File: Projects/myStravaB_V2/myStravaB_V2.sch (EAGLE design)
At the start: 103 parts, among them IC1 TPS63051RMWT, Q2 BSS138BKW, T1 BC847, T2 BC847, U1 FXOS8700CQR1, U2 MCP73831, U4 NRF52840, Y2 16MHz, Y3 32.768kHz

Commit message: Final design
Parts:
- added U$8: NET_CONN, NET_CONN:NET_CONN
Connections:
- new net N$10: C35.2, U$8.2, U4.VSS_PA
- net GND: now also U$8.1; no longer C35.2, U4.VSS_PA

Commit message: Added speaker
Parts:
- added C18: 1uF, rcl:C-EUC0603
- added C19: DNP, rcl:C-EUC0805
- added R28: 10k, rcl:R-US_R0603
- added R29: 330, rcl:R-US_R0603
- added T3: BC847, transistor:BC847
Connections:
- removed net XX: U4.P26
- new net N$11: R28.2, T3.B
- new net N$18: C18.2, C19.2
- new net N$6: C18.1, R29.1, T3.C
- new net SPK_IN: R28.1, U4.P26
- net GND: now also C19.1, T3.E
- net VCC: now also R29.2

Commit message: Some fuckups corrected
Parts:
- C35: value 820pF -> 0.8pF
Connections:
- removed net YY: U4.P4
- net DEC2: now also U4.DEC2; no longer U4.DEC2B
- net DEC4_6: now also U4.DEC6; no longer U4.DEC2
- net KILL_NRF: now also U4.P1.10
- net NEO_PIN: now also U4.P4
- net PPS: no longer U4.P6
- net USB_PRES: now also U4.P6

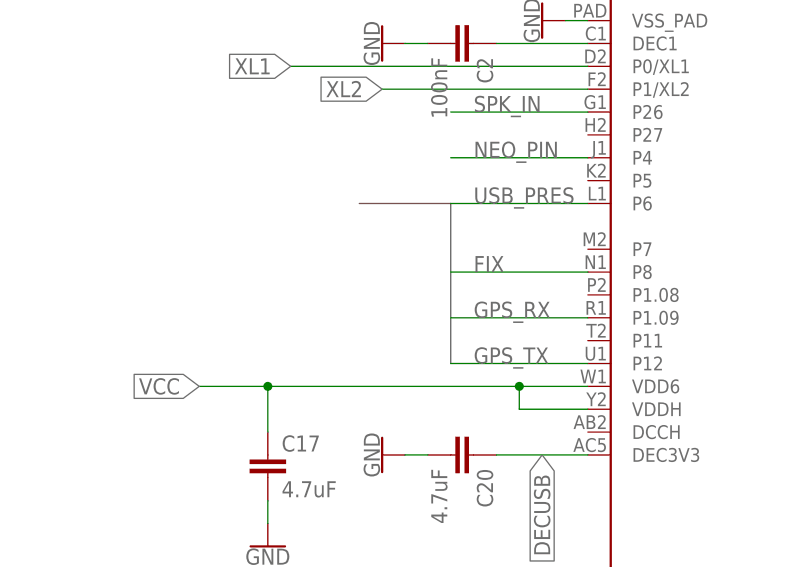
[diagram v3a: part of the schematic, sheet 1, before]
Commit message: Changed packages Routed USB_PRES
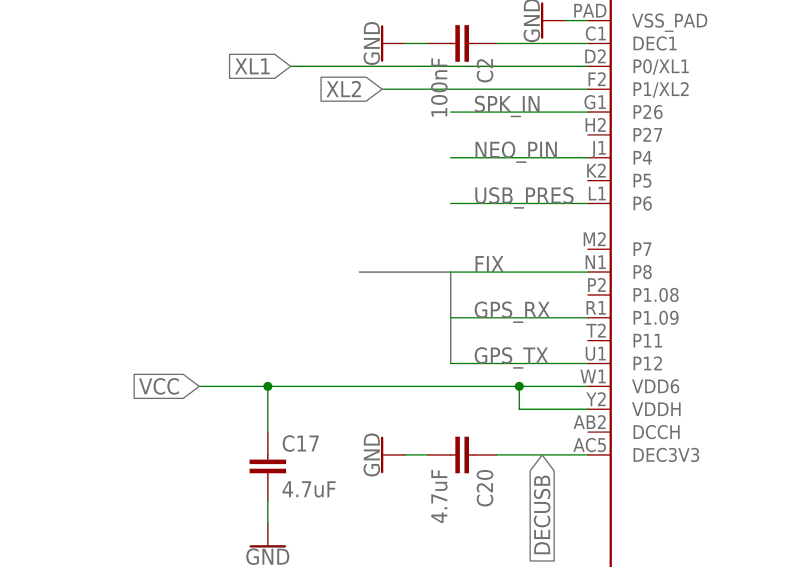
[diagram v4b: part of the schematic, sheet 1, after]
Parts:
- C2, C24, C26, C29: device rcl:C-EUC0402 -> rcl:C-EUC0603
- R1, R2: device rcl:R-US_R0402 -> rcl:R-US_R0603

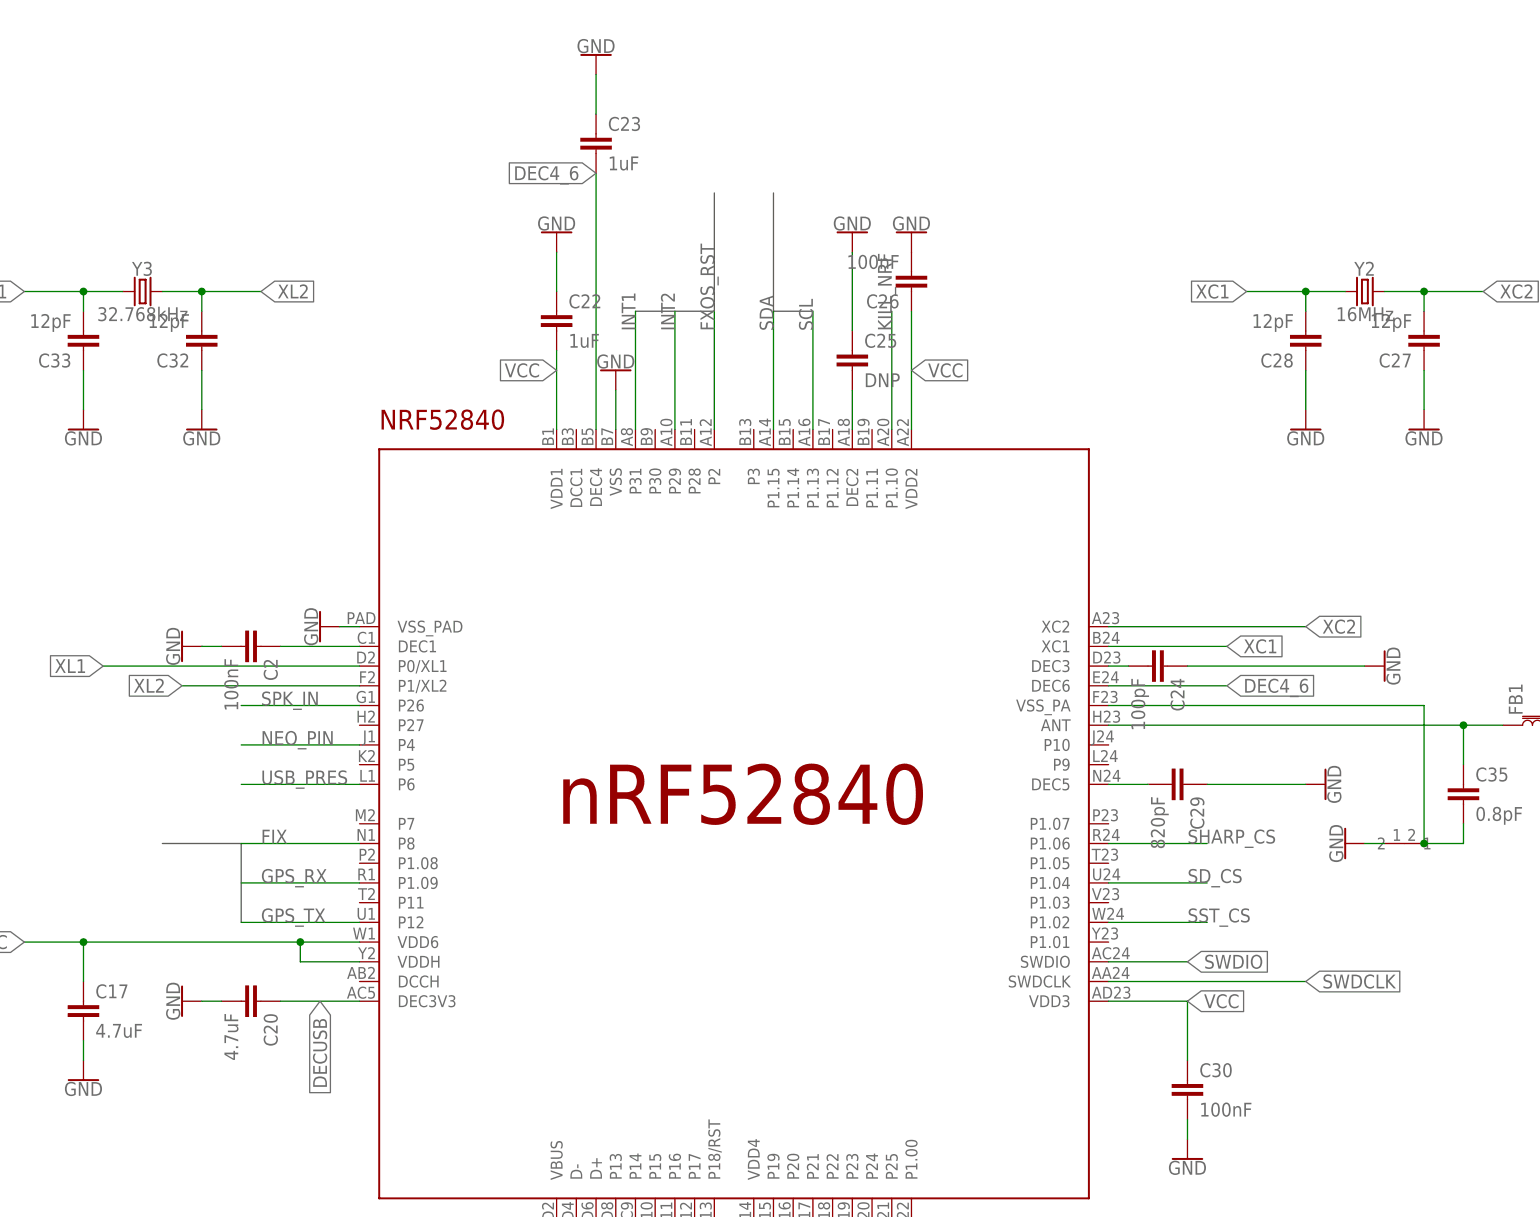
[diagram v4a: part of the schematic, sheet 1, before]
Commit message: Corrected mistakes on myStravaV10
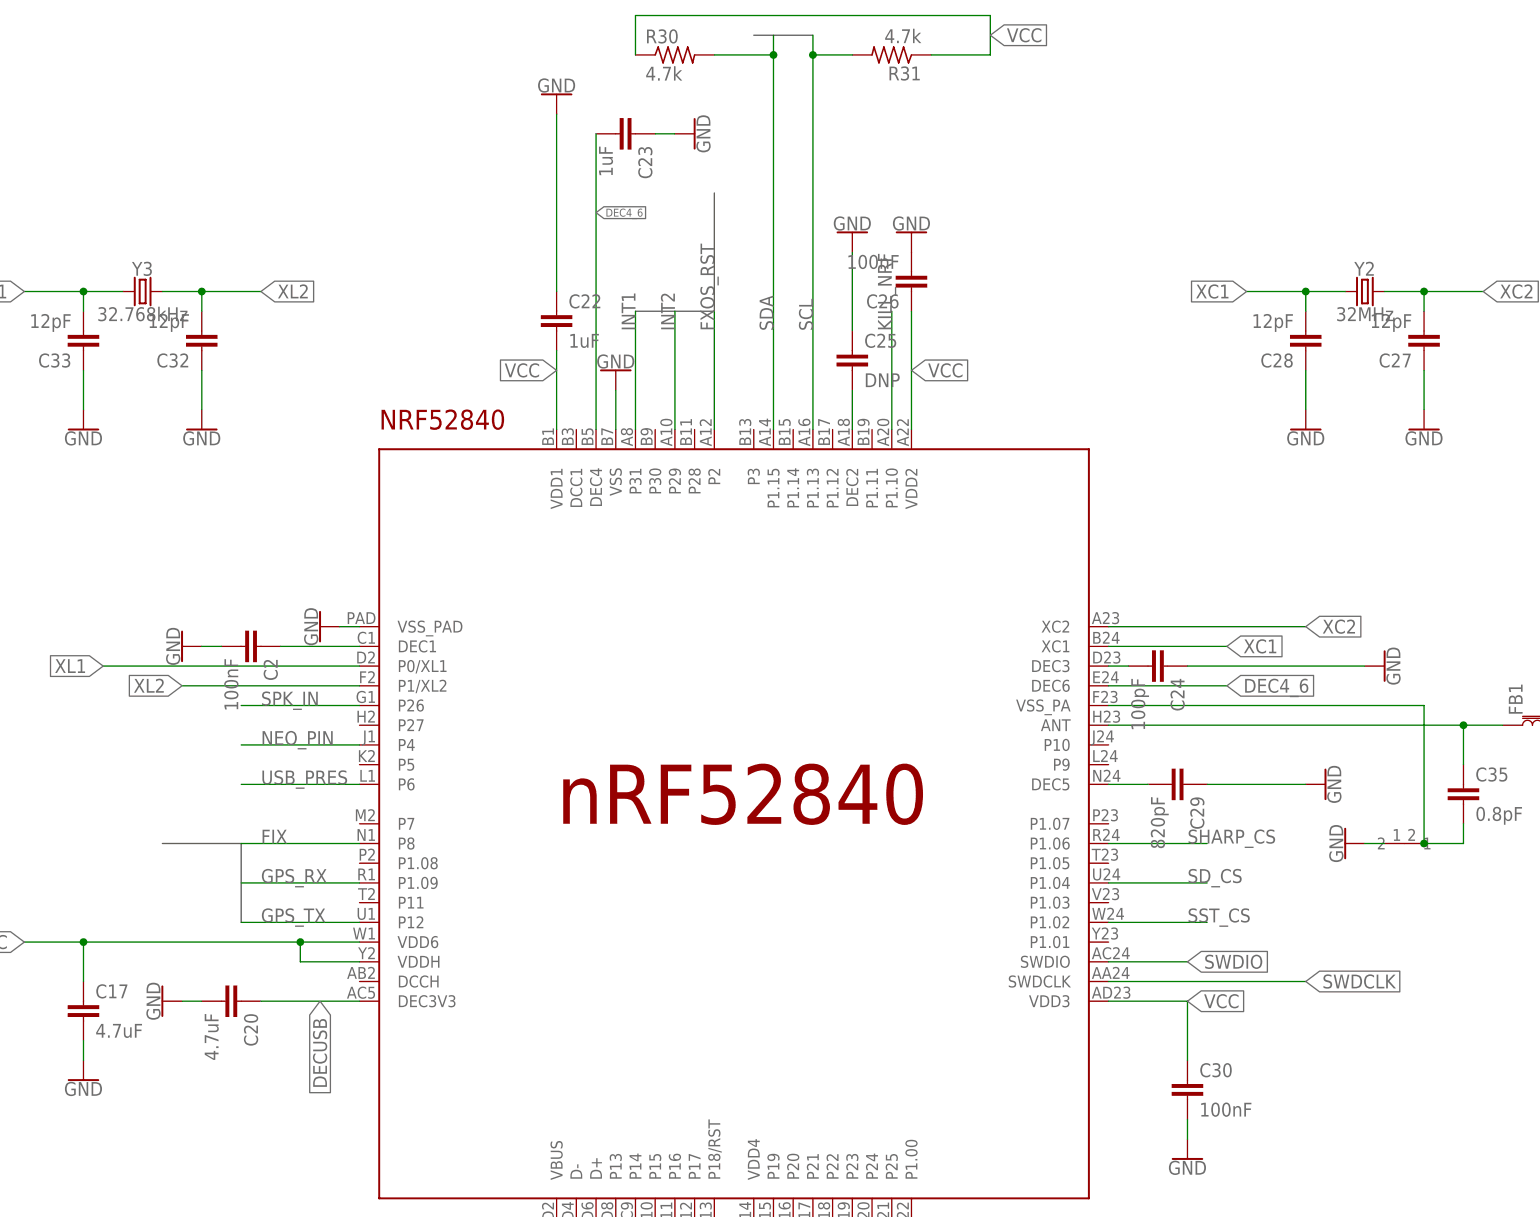
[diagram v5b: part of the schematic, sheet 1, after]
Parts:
- added R30, R31: 4.7k, rcl:R-US_R0603
- Y2: value 16MHz -> 32MHz
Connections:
- net SCL: now also R31.2
- net SDA: now also R30.2
- net VCC: now also R30.1, R31.1
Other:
- moved on the sheet: C20, C23

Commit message: Improved version of the bike GPS
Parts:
- removed C18: 1uF, rcl:C-EUC0603
- removed C19: DNP, rcl:C-EUC0805
- removed D2: BAT54C, diode:BAT54C
- removed R28: 10k, rcl:R-US_R0603
- removed R29: 330, rcl:R-US_R0603
- removed R4: 4.7k, SparkFun-Resistors:4.7KOHM-0603-1/10W-1%
- removed R5: 10k, SparkFun-Resistors:4.7KOHM-0603-1/10W-1%
- removed T3: BC847, transistor:BC847
- removed U$10: DM3AT, HIROSE-DM3AT:DM3AT
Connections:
- removed net HW_R: C41.1, U$5.HW_R
- removed net HW_S: C40.1, U$5.HW_S
- removed net N$11: R28.2, T3.B
- removed net N$18: C18.2, C19.2
- removed net N$6: C18.1, R29.1, T3.C
- removed net N$8: U$1G$1.G, U$1G$2.S
- removed net SD_CS: U$10.CS, U4.P1.04
- removed net SHARP_CS: U$16.CS, U4.P1.06
- removed net SPK_IN: R28.1, U4.P26
- removed net SW_VBAT: C4.2, D2.A2, L4.VDD, R10.1, R18.2, U$1G$1.S
- removed net USB_PRES: R4.1, R5.2, U4.P6
- new net A2: U4.P31
- new net A3: U4.P29
- new net A99: U4.P10
- new net GPS_RST: C41.1, U$5.HW_R, U4.P4
- new net GPS_STDBY: C40.1, U$5.HW_S, U4.P6
- new net LS027_CS: U$16.CS, U4.P24
- new net LS027_MO: U$16.MOSI, U4.P22
- new net LS027_SCK: U$16.SCLK, U4.P20
- net GND: now also U$1G$1.S; no longer C19.1, R5.1, T3.E, U$10.GND, U$1G$2.D
- net INT1: no longer U4.P31
- net INT2: no longer U4.P29
- net N$15: now also U$1G$1.G; no longer U$1G$2.G
- net N$9: now also U$1G$1.D, U$1G$2.G
- net NEO_PIN: now also U4.P26; no longer U4.P4
- net PW_EN: now also C4.2, L4.VDD, R10.1, R18.2, U$1G$2.D; no longer D2.CC
- net SPI_MI: now also U4.P1.06; no longer U$10.MISO, U4.P24
- net SPI_MO: now also U4.P9; no longer U$10.MOSI, U$16.MOSI, U4.P22
- net SPI_SCK: now also U4.P1.04; no longer U$10.CLK, U$16.SCLK, U4.P20
- net VBAT: now also U$1G$2.S; no longer U$1G$1.D
- net VCC: no longer R29.2, U$10.VCC
- net VUSB: no longer D2.A1, R4.2

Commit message: Board routed completely:to be checked
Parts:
- removed R6, R7: 4.7k, SparkFun-Resistors:4.7KOHM-0603-1/10W-1%
- added C18: 0.1uF, SparkFun-Capacitors:4.7UF0603
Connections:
- removed net A3: U4.P29
- removed net A99: U4.P10
- removed net N$4: R6.2, U$2.WP
- removed net N$5: R7.1, U$2.HOLD
- new net SST_HOLD: U$2.HOLD, U4.P1.00
- new net SST_WP: U$2.WP, U4.P9
- net GND: now also C18.2
- net INT1: now also U4.P29
- net PIN_BCK: no longer U4.P1.00
- net SPI_MI: now also U4.P10; no longer U4.P1.06
- net SPI_MO: now also U4.P1.02; no longer U4.P9
- net SST_CS: now also U4.P1.06; no longer U4.P1.02
- net VCC: now also C18.1; no longer R6.1, R7.2
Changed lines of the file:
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@@
 <part name="U$2" library="FlashMem" deviceset="FLASH" device=""/>
 <part name="GND39" library="SparkFun-PowerSymbols" deviceset="GND" device=""/>
-<part name="R6" library="SparkFun-Resistors" deviceset="4.7KOHM" device="-0603-1/10W-1%" value="4.7k"/>
-<part name="R7" library="SparkFun-Resistors" deviceset="4.7KOHM" device="-0603-1/10W-1%" value="4.7k"/>
 <part name="U4" library="nRF52840" deviceset="NRF52840" device="" value="NRF52840">
 <attribute name="SPICEPREFIX" value="X"/>
@@
 <part name="R30" library="rcl" library_urn="urn:adsk.eagle:library:334" deviceset="R-US_" device="R0603" package3d_urn="urn:adsk.eagle:package:23555/2" value="4.7k"/>
 <part name="R31" library="rcl" library_urn="urn:adsk.eagle:library:334" deviceset="R-US_" device="R0603" package3d_urn="urn:adsk.eagle:package:23555/2" value="4.7k"/>
+<part name="C18" library="SparkFun-Capacitors" deviceset="4.7UF" device="0603" value="0.1uF"/>
+<part name="GND17" library="SparkFun-PowerSymbols" deviceset="GND" device=""/>
 </parts>
 <sheets>
@@
 </segment>
 </net>
-<net name="PIN_BCK" class="0">
-<segment>
-<pinref part="U4" gate="G$1" pin="P1.00"/>
-<wire x1="12.7" y1="261.62" x2="12.7" y2="246.38" width="0.1524" layer="91"/>
-<label x="12.7" y="248.92" size="1.778" layer="95" rot="R90"/>
-</segment>
-</net>
-<net name="SST_CS" class="0">
-<segment>
-<pinref part="U4" gate="G$1" pin="P1.02"/>
-<wire x1="38.1" y1="299.72" x2="50.8" y2="299.72" width="0.1524" layer="91"/>
-<label x="45.72" y="299.72" size="1.778" layer="95"/>
-</segment>
-</net>
 <net name="LS027_CS" class="0">
 <segment>
@@
 </segment>
 </net>
+<net name="A2" class="0">
+<segment>
+<pinref part="U4" gate="G$1" pin="P31"/>
+<wire x1="-22.86" y1="363.22" x2="-22.86" y2="378.46" width="0.1524" layer="91"/>
+<label x="-22.86" y="375.92" size="1.778" layer="95" rot="R90"/>
+</segment>
+</net>
+<net name="INT1" class="0">
+<segment>
+<pinref part="U4" gate="G$1" pin="P29"/>
+<wire x1="-17.78" y1="363.22" x2="-17.78" y2="378.46" width="0.1524" layer="91"/>
+<label x="-17.78" y="375.92" size="1.778" layer="95" rot="R90"/>
+</segment>
+</net>
+<net name="GPS_STDBY" class="0">
+<segment>
+<pinref part="U4" gate="G$1" pin="P6"/>
+<wire x1="-58.42" y1="317.5" x2="-73.66" y2="317.5" width="0.1524" layer="91"/>
+<label x="-71.12" y="317.5" size="1.778" layer="95"/>
+</segment>
+</net>
+<net name="SPI_MO" class="0">
+<segment>
+<pinref part="U4" gate="G$1" pin="P1.02"/>
+<wire x1="38.1" y1="299.72" x2="50.8" y2="299.72" width="0.1524" layer="91"/>
+<label x="45.72" y="299.72" size="1.778" layer="95"/>
+</segment>
+</net>
+<net name="LS027_MO" class="0">
+<segment>
+<pinref part="U4" gate="G$1" pin="P22"/>
+<wire x1="2.54" y1="261.62" x2="2.54" y2="246.38" width="0.1524" layer="91"/>
+<label x="2.54" y="248.92" size="1.778" layer="95" rot="R90"/>
+</segment>
+</net>
+<net name="LS027_SCK" class="0">
+<segment>
+<pinref part="U4" gate="G$1" pin="P20"/>
+<wire x1="-2.54" y1="261.62" x2="-2.54" y2="246.38" width="0.1524" layer="91"/>
+<label x="-2.54" y="248.92" size="1.778" layer="95" rot="R90"/>
+</segment>
+</net>
+<net name="GPS_RST" class="0">
+<segment>
+<pinref part="U4" gate="G$1" pin="P4"/>
+<wire x1="-58.42" y1="322.58" x2="-73.66" y2="322.58" width="0.1524" layer="91"/>
+<label x="-71.12" y="322.58" size="1.778" layer="95"/>
+</segment>
+</net>
+<net name="SST_CS" class="0">
+<segment>
+<pinref part="U4" gate="G$1" pin="P1.06"/>
+<wire x1="38.1" y1="309.88" x2="50.8" y2="309.88" width="0.1524" layer="91"/>
+<label x="45.72" y="309.88" size="1.778" layer="95"/>
+</segment>
+</net>
 <net name="SPI_SCK" class="0">
 <segment>
@@
 </segment>
 </net>
-<net name="A2" class="0">
-<segment>
-<pinref part="U4" gate="G$1" pin="P31"/>
-<wire x1="-22.86" y1="363.22" x2="-22.86" y2="378.46" width="0.1524" layer="91"/>
-<label x="-22.86" y="375.92" size="1.778" layer="95" rot="R90"/>
-</segment>
-</net>
-<net name="A3" class="0">
-<segment>
-<pinref part="U4" gate="G$1" pin="P29"/>
-<wire x1="-17.78" y1="363.22" x2="-17.78" y2="378.46" width="0.1524" layer="91"/>
-<label x="-17.78" y="375.92" size="1.778" layer="95" rot="R90"/>
-</segment>
-</net>
-<net name="GPS_STDBY" class="0">
-<segment>
-<pinref part="U4" gate="G$1" pin="P6"/>
-<wire x1="-58.42" y1="317.5" x2="-73.66" y2="317.5" width="0.1524" layer="91"/>
-<label x="-71.12" y="317.5" size="1.778" layer="95"/>
-</segment>
-</net>
-<net name="A99" class="0">
+<net name="SPI_MI" class="0">
 <segment>
 <pinref part="U4" gate="G$1" pin="P10"/>
@@
 </segment>
 </net>
-<net name="SPI_MO" class="0">
+<net name="SST_WP" class="0">
 <segment>
 <pinref part="U4" gate="G$1" pin="P9"/>
@@
 </segment>
 </net>
-<net name="LS027_MO" class="0">
-<segment>
-<pinref part="U4" gate="G$1" pin="P22"/>
-<wire x1="2.54" y1="261.62" x2="2.54" y2="246.38" width="0.1524" layer="91"/>
-<label x="2.54" y="248.92" size="1.778" layer="95" rot="R90"/>
-</segment>
-</net>
-<net name="LS027_SCK" class="0">
-<segment>
-<pinref part="U4" gate="G$1" pin="P20"/>
-<wire x1="-2.54" y1="261.62" x2="-2.54" y2="246.38" width="0.1524" layer="91"/>
-<label x="-2.54" y="248.92" size="1.778" layer="95" rot="R90"/>
-</segment>
-</net>
-<net name="GPS_RST" class="0">
-<segment>
-<pinref part="U4" gate="G$1" pin="P4"/>
-<wire x1="-58.42" y1="322.58" x2="-73.66" y2="322.58" width="0.1524" layer="91"/>
-<label x="-71.12" y="322.58" size="1.778" layer="95"/>
-</segment>
-</net>
-<net name="SPI_MI" class="0">
-<segment>
-<pinref part="U4" gate="G$1" pin="P1.06"/>
-<wire x1="38.1" y1="309.88" x2="50.8" y2="309.88" width="0.1524" layer="91"/>
-<label x="45.72" y="309.88" size="1.778" layer="95"/>
+<net name="SST_HOLD" class="0">
+<segment>
+<pinref part="U4" gate="G$1" pin="P1.00"/>
+<wire x1="12.7" y1="261.62" x2="12.7" y2="246.38" width="0.1524" layer="91"/>
+<label x="12.7" y="248.92" size="1.778" layer="95" rot="R90"/>
 </segment>
 </net>
@@
 <attribute name="VALUE" x="-10.414" y="7.62" size="1.778" layer="96" rot="R270" align="top-center"/>
 </instance>
-<instance part="R6" gate="G$1" x="-15.24" y="12.7" smashed="yes">
-<attribute name="NAME" x="-15.24" y="14.224" size="1.778" layer="95" font="vector" align="bottom-center"/>
-<attribute name="VALUE" x="-15.24" y="11.176" size="1.778" layer="96" font="vector" align="top-center"/>
-</instance>
-<instance part="R7" gate="G$1" x="50.8" y="17.78" smashed="yes">
-<attribute name="NAME" x="50.8" y="19.304" size="1.778" layer="95" font="vector" align="bottom-center"/>
-<attribute name="VALUE" x="50.8" y="16.256" size="1.778" layer="96" font="vector" align="top-center"/>
-</instance>
 <instance part="BTNG1" gate="G$1" x="-111.76" y="121.92" smashed="yes"/>
 <instance part="BTNC1" gate="G$1" x="-111.76" y="104.14" smashed="yes"/>
 <instance part="BTND1" gate="G$1" x="-111.76" y="86.36" smashed="yes"/>
+<instance part="C18" gate="G$1" x="45.72" y="30.48" smashed="yes" rot="R180">
+<attribute name="NAME" x="44.196" y="27.559" size="1.778" layer="95" font="vector" rot="R180"/>
+<attribute name="VALUE" x="44.196" y="32.639" size="1.778" layer="96" font="vector" rot="R180"/>
+</instance>
+<instance part="GND17" gate="1" x="45.72" y="38.1" smashed="yes" rot="R180">
+<attribute name="VALUE" x="45.72" y="38.354" size="1.778" layer="96" rot="R180" align="top-center"/>
+</instance>
 </instances>
 <busses>
@@
 <pinref part="BTND1" gate="G$1" pin="P$1"/>
 <label x="-142.24" y="86.36" size="1.016" layer="95" rot="R180" xref="yes"/>
+</segment>
+<segment>
+<pinref part="GND17" gate="1" pin="GND"/>
+<pinref part="C18" gate="G$1" pin="2"/>
+<wire x1="45.72" y1="35.56" x2="45.72" y2="33.02" width="0.1524" layer="91"/>
 </segment>
 </net>
@@
 <segment>
 <pinref part="U$2" gate="G$1" pin="VDD"/>
-<wire x1="33.02" y1="22.86" x2="53.34" y2="22.86" width="0.1524" layer="91"/>
+<wire x1="33.02" y1="22.86" x2="45.72" y2="22.86" width="0.1524" layer="91"/>
 <label x="53.34" y="22.86" size="1.778" layer="95" xref="yes"/>
-</segment>
-<segment>
-<pinref part="R6" gate="G$1" pin="1"/>
-<wire x1="-20.32" y1="12.7" x2="-27.94" y2="12.7" width="0.1524" layer="91"/>
-<label x="-27.94" y="12.7" size="1.778" layer="95" rot="R180" xref="yes"/>
-</segment>
-<segment>
-<pinref part="R7" gate="G$1" pin="2"/>
-<wire x1="55.88" y1="17.78" x2="66.04" y2="17.78" width="0.1524" layer="91"/>
-<label x="66.04" y="17.78" size="1.778" layer="95" xref="yes"/>
+<pinref part="C18" gate="G$1" pin="1"/>
+<wire x1="45.72" y1="22.86" x2="53.34" y2="22.86" width="0.1524" layer="91"/>
+<wire x1="45.72" y1="25.4" x2="45.72" y2="22.86" width="0.1524" layer="91"/>
+<junction x="45.72" y="22.86"/>
 </segment>
 </net>
@@
 </segment>
 </net>
-<net name="N$4" class="0">
+<net name="SST_WP" class="0">
 <segment>
 <pinref part="U$2" gate="G$1" pin="WP"/>
-<wire x1="2.54" y1="12.7" x2="-10.16" y2="12.7" width="0.1524" layer="91"/>
-<pinref part="R6" gate="G$1" pin="2"/>
-</segment>
-</net>
-<net name="N$5" class="0">
+<wire x1="2.54" y1="12.7" x2="-12.7" y2="12.7" width="0.1524" layer="91"/>
+<label x="-12.7" y="12.7" size="1.778" layer="95" rot="R180" xref="yes"/>
+</segment>
+</net>
+<net name="SST_HOLD" class="0">
 <segment>
 <pinref part="U$2" gate="G$1" pin="HOLD"/>
-<wire x1="33.02" y1="17.78" x2="45.72" y2="17.78" width="0.1524" layer="91"/>
-<pinref part="R7" gate="G$1" pin="1"/>
-</segment>
-</net>
+<wire x1="33.02" y1="17.78" x2="53.34" y2="17.78" width="0.1524" layer="91"/>
+<label x="53.34" y="17.78" size="1.778" layer="95" xref="yes"/>
+</segment>
+</net>
